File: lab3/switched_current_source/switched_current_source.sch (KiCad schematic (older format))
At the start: 52 parts, among them J1 Conn_01x02_Male, J2 Conn_01x02_Male, J3 Conn_01x02_Male, J4 Conn_01x07_Male, Q1 MMBT3904, Q2 MMBT3906, Q3 MMBT3906, Q4 MMBT3904, Q5 J310, Q6 J310, U1 LM358, U2 LM358, U3 LM358, U4 LM358

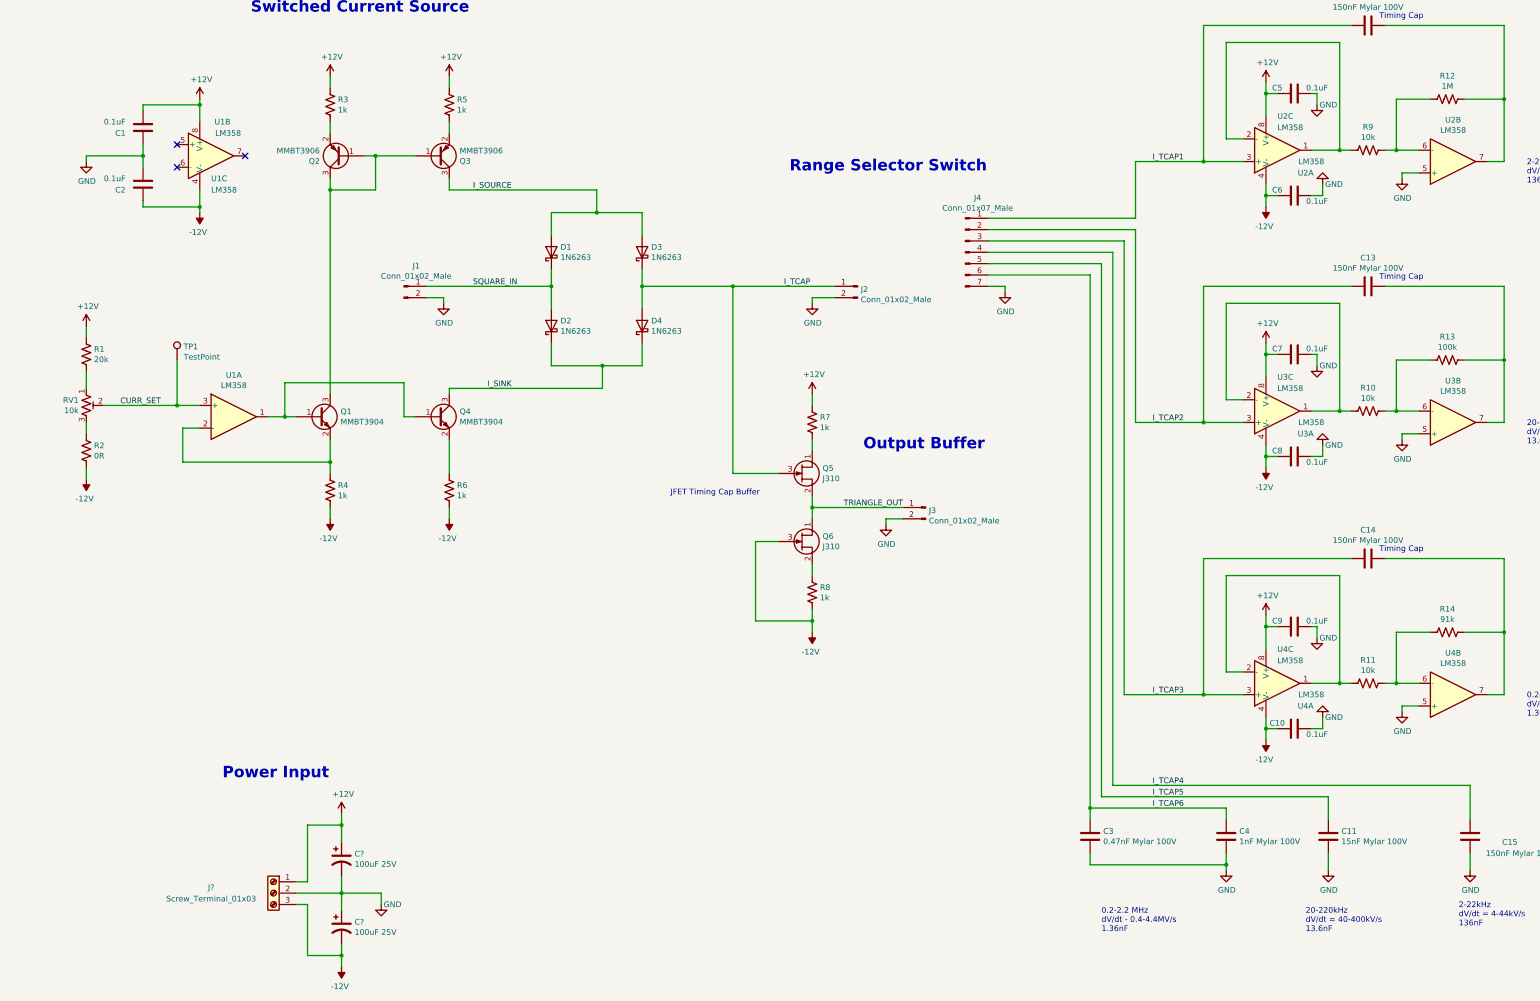
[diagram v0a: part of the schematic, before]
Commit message: Switched Current Source Rev A
* Update resistor values for cap miller multipliers.
* Update ibom.
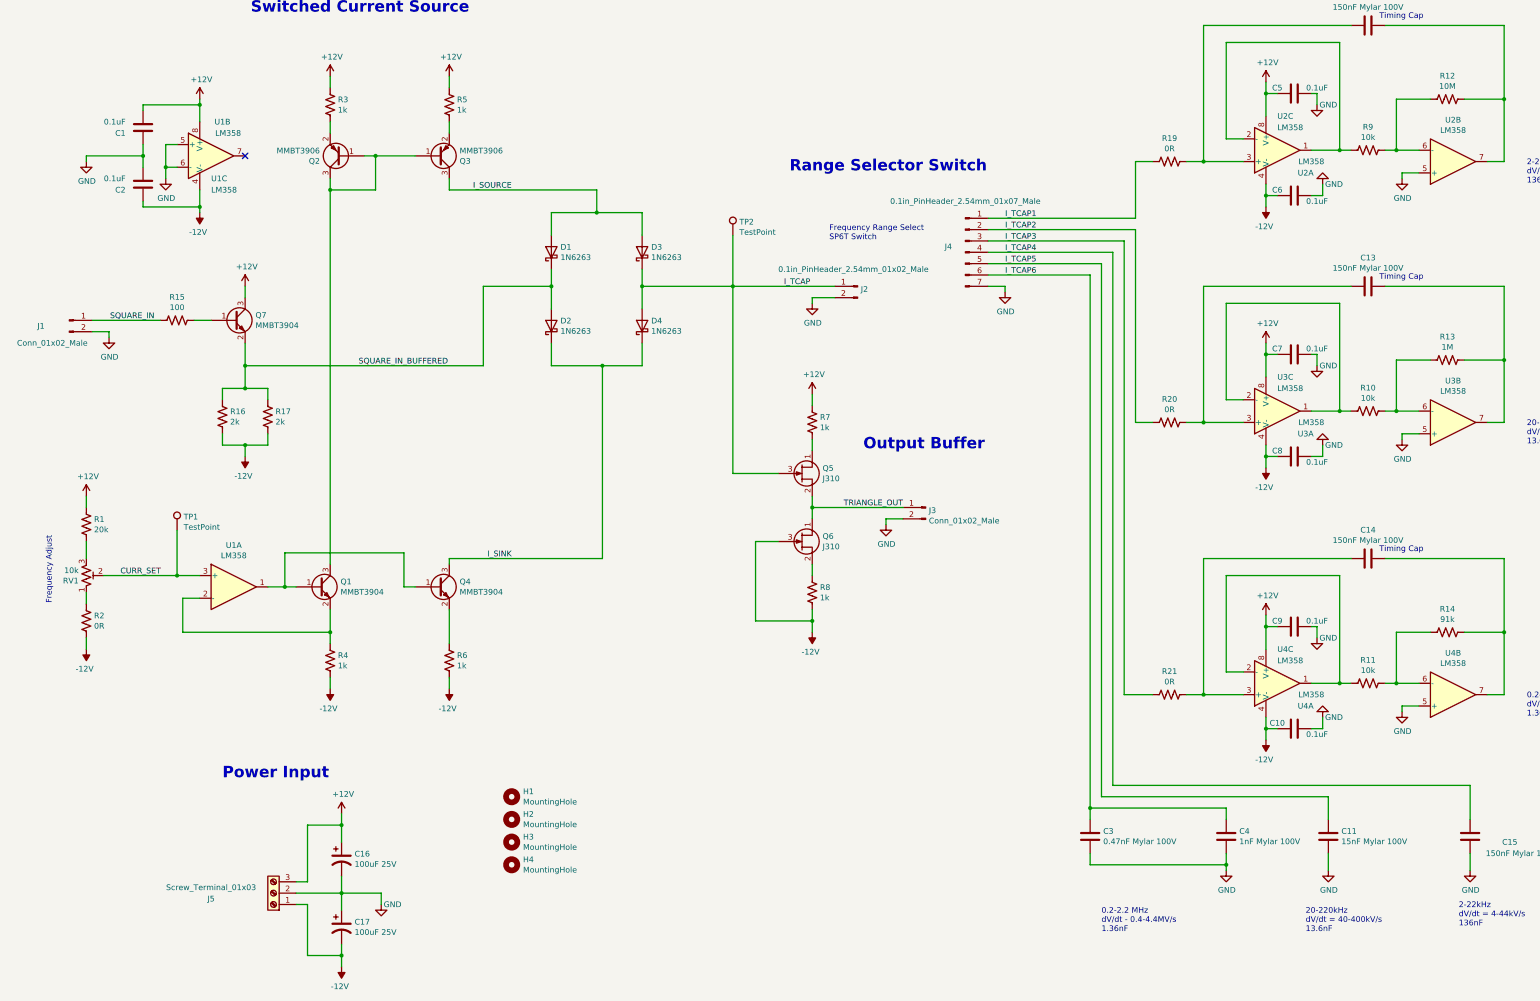
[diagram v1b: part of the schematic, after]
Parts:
- added H1, H2, H3, H4: MountingHole, MountingHole:MountingHole_3.2mm_M3, symbol Mechanical:MountingHole
- added Q7: MMBT3904, Package_TO_SOT_SMD:SOT-23, symbol Transistor_BJT:MMBT3904
- added R15: 100, Resistor_SMD:R_0805_2012Metric, symbol Device:R_US
- added R16, R17: 2k, Resistor_SMD:R_0805_2012Metric, symbol Device:R_US
- added R19, R20, R21: 0R, Resistor_SMD:R_0805_2012Metric, symbol Device:R_US
- added TP2: TestPoint, TestPoint:TestPoint_THTPad_D2.0mm_Drill1.0mm, symbol Connector:TestPoint
- C10, C5, C6, C7, C8, C9: footprint (none) -> Capacitor_SMD:C_0805_2012Metric
- C11, C3, C4: footprint (none) -> Capacitor_THT:C_Rect_L7.0mm_W2.5mm_P5.00mm
- C12, C13, C14, C15: footprint (none) -> Capacitor_THT:C_Rect_L10.0mm_W4.0mm_P7.50mm_MKS4
- C16, C17: renamed from C?; footprint (none) -> Capacitor_THT:CP_Radial_D5.0mm_P2.00mm
- J2: value Conn_01x02_Male -> 0.1in_PinHeader_2.54mm_01x02_Male
- J4: value Conn_01x07_Male -> 0.1in_PinHeader_2.54mm_01x07_Male; footprint (none) -> Connector_PinHeader_2.54mm:PinHeader_1x07_P2.54mm_Vertical
- J5: renamed from J?; footprint (none) -> TerminalBlock_Phoenix:TerminalBlock_Phoenix_MKDS-1,5-3-5.08_1x03_P5.08mm_Horizontal
- Q5, Q6: footprint (none) -> Package_TO_SOT_THT:TO-92
- R10, R11, R14, R2, R7, R8, R9: footprint (none) -> Resistor_SMD:R_0805_2012Metric
- R12: value 1M -> 10M; footprint (none) -> Resistor_SMD:R_0805_2012Metric
- R13: value 100k -> 1M; footprint (none) -> Resistor_SMD:R_0805_2012Metric
- RV1: footprint (none) -> Potentiometer_THT:Potentiometer_Alps_RK163_Single_Horizontal
- TP1: footprint (none) -> TestPoint:TestPoint_THTPad_D2.0mm_Drill1.0mm
- U2, U3, U4: footprint (none) -> Package_DIP:DIP-8_W7.62mm
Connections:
- net +12V: now also J5.3 (Pin_3), Q7.3 (C); no longer J5.1 (Pin_1)
- net -12V: now also J5.1 (Pin_1), R16.2, R17.2; no longer J5.3 (Pin_3)
- net GND: now also U1.5 (+), U1.6 (-)
- net I_TCAP: now also TP2.1
- net I_TCAP1: now also R19.2; no longer C12.2, U2.3 (+)
- net I_TCAP2: now also R20.2; no longer C13.2, U3.3 (+)
- net I_TCAP3: now also R21.2; no longer C14.2, U4.3 (+)
- net SQUARE_IN: now also R15.2; no longer D1.1 (K), D2.2 (A)
- net at R1.2: now also RV1.3; no longer RV1.1
- net at R2.1: now also RV1.1; no longer RV1.3
- new net: C13.2, R20.1, U3.3 (+)
- new net: C12.2, R19.1, U2.3 (+)
- new net: Q7.1 (B), R15.1
- new net: C14.2, R21.1, U4.3 (+)
- new net SQUARE_IN_BUFFERED: D1.1 (K), D2.2 (A), Q7.2 (E), R16.1, R17.1
- no-connect marks 3 -> 1
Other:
- note added: "Frequency Adjust"
- note added: "Frequency Range Select\nSP6T Switch"
- note removed: "JFET Timing Cap Buffer"
- moved on the sheet: J1, Q1, Q4, R1, R2, R4, R6, RV1, TP1, U1A

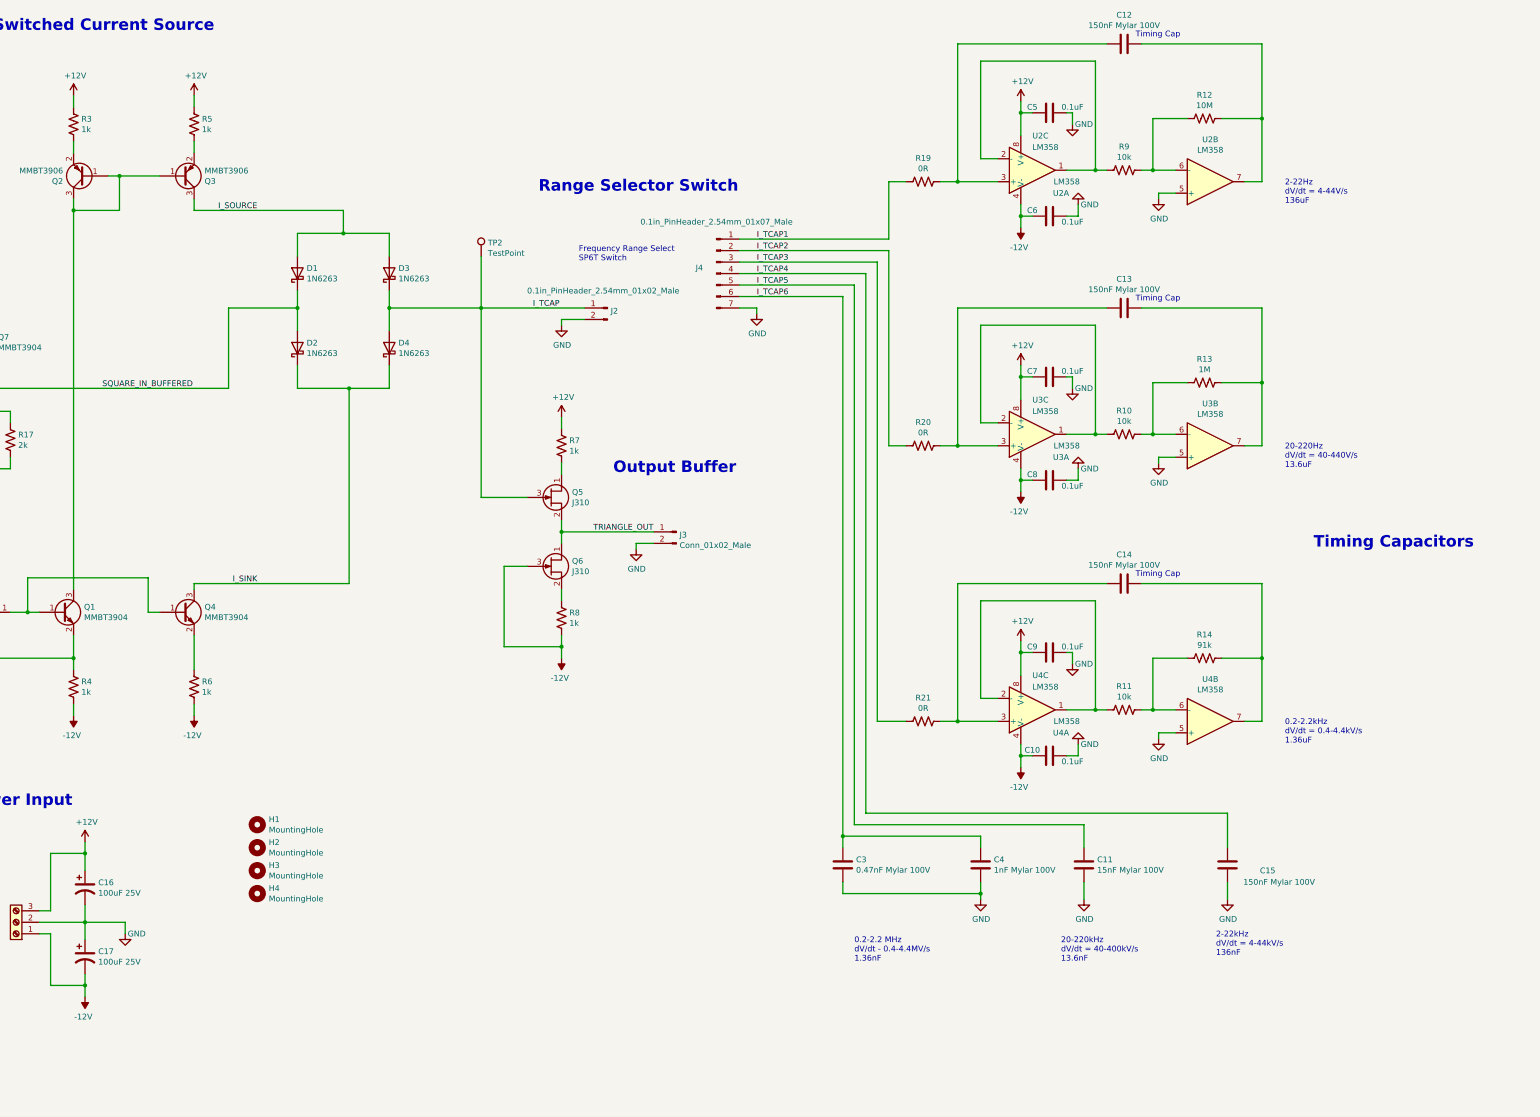
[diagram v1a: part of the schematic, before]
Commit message: Finish function generator
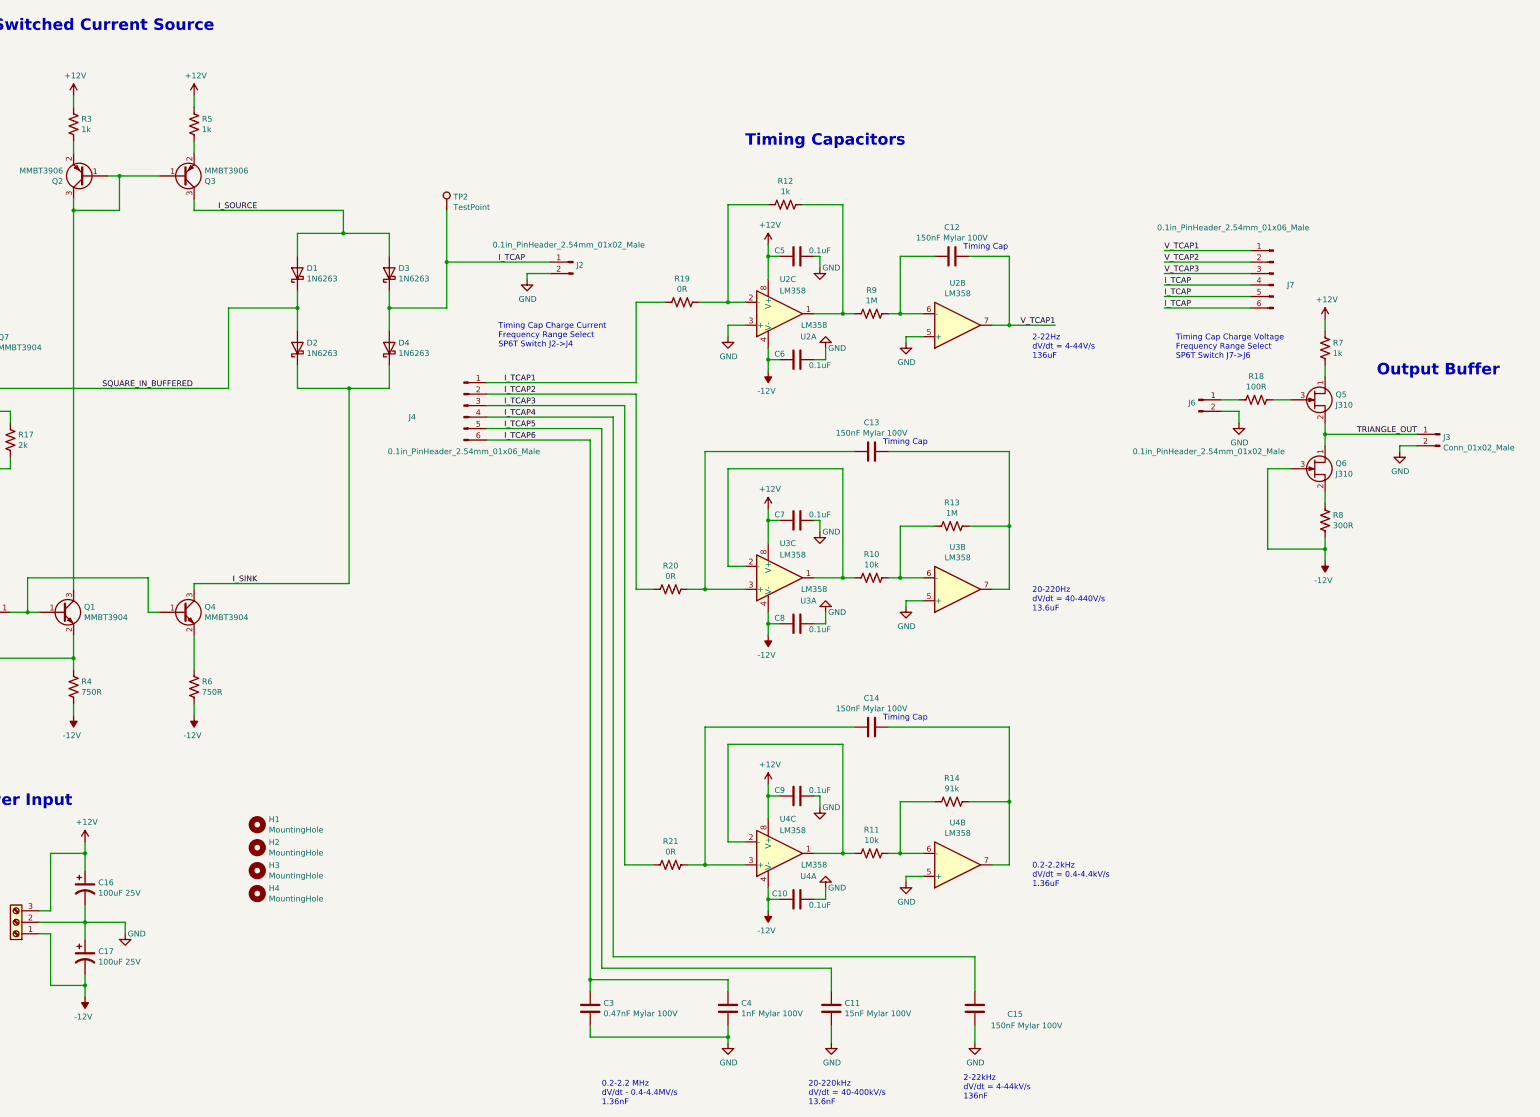
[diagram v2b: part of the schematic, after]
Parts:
- removed J4: 0.1in_PinHeader_2.54mm_01x07_Male, Connector_PinHeader_2.54mm:PinHeader_1x07_P2.54mm_Vertical, symbol Connector:Conn_01x07_Male
- added J4, J7: 0.1in_PinHeader_2.54mm_01x06_Male, symbol Connector:Conn_01x06_Male
- added J6: 0.1in_PinHeader_2.54mm_01x02_Male, Connector_PinHeader_2.54mm:PinHeader_1x02_P2.54mm_Vertical, symbol Connector:Conn_01x02_Male
- added R18: 100R, symbol Device:R_US
- R12: value 10M -> 1k; footprint Resistor_SMD:R_0805_2012Metric -> (none)
- R4, R6: value 1k -> 750R
- R8: value 1k -> 300R
- R9: value 10k -> 1M
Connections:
- net GND: now also U2.3 (+), J6.2 (Pin_2)
- net I_TCAP: now also J7.4 (Pin_4), J7.5 (Pin_5), J7.6 (Pin_6); no longer Q5.3 (G)
- net I_TCAP1: now also J4.1 (Pin_1)
- net I_TCAP2: now also J4.2 (Pin_2)
- net I_TCAP3: now also J4.3 (Pin_3)
- net I_TCAP4: now also J4.4 (Pin_4)
- net I_TCAP5: now also J4.5 (Pin_5)
- net I_TCAP6: now also J4.6 (Pin_6)
- net at R9.2, U2.1: now also R12.1; no longer U2.2 (-)
- net at R9.1, U2.6 (-): now also C12.2; no longer R12.2
- net V_TCAP1: now reaches C12.1, U2.7
- net V_TCAP1: now also J7.1 (Pin_1); no longer R12.1
- new net: Q5.3 (G), R18.1
- new net: R12.2, R19.1, U2.2 (-)
- new net: J6.1 (Pin_1), R18.2
- new net V_TCAP2: J7.2 (Pin_2)
- new net V_TCAP3: J7.3 (Pin_3)
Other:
- note added: "Timing Cap Charge Current\nFrequency Range Select\nSP6T Switch J2->J4"
- note added: "Timing Cap Charge Voltage\nFrequency Range Select\nSP6T Switch J7->J6"
- note removed: "Frequency Range Select\nSP6T Switch"
- note removed: "Range Selector Switch"
- moved on the sheet: C10, C11, C12, C13, C14, C15, C3, C4, C5, C6, C7, C8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
